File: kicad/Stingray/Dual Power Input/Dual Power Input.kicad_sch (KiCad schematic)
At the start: 16 parts, among them J2 Screw_Terminal_01x12, SW1 SW_SPST, U1 TMLM04115, U2 TMLM04115

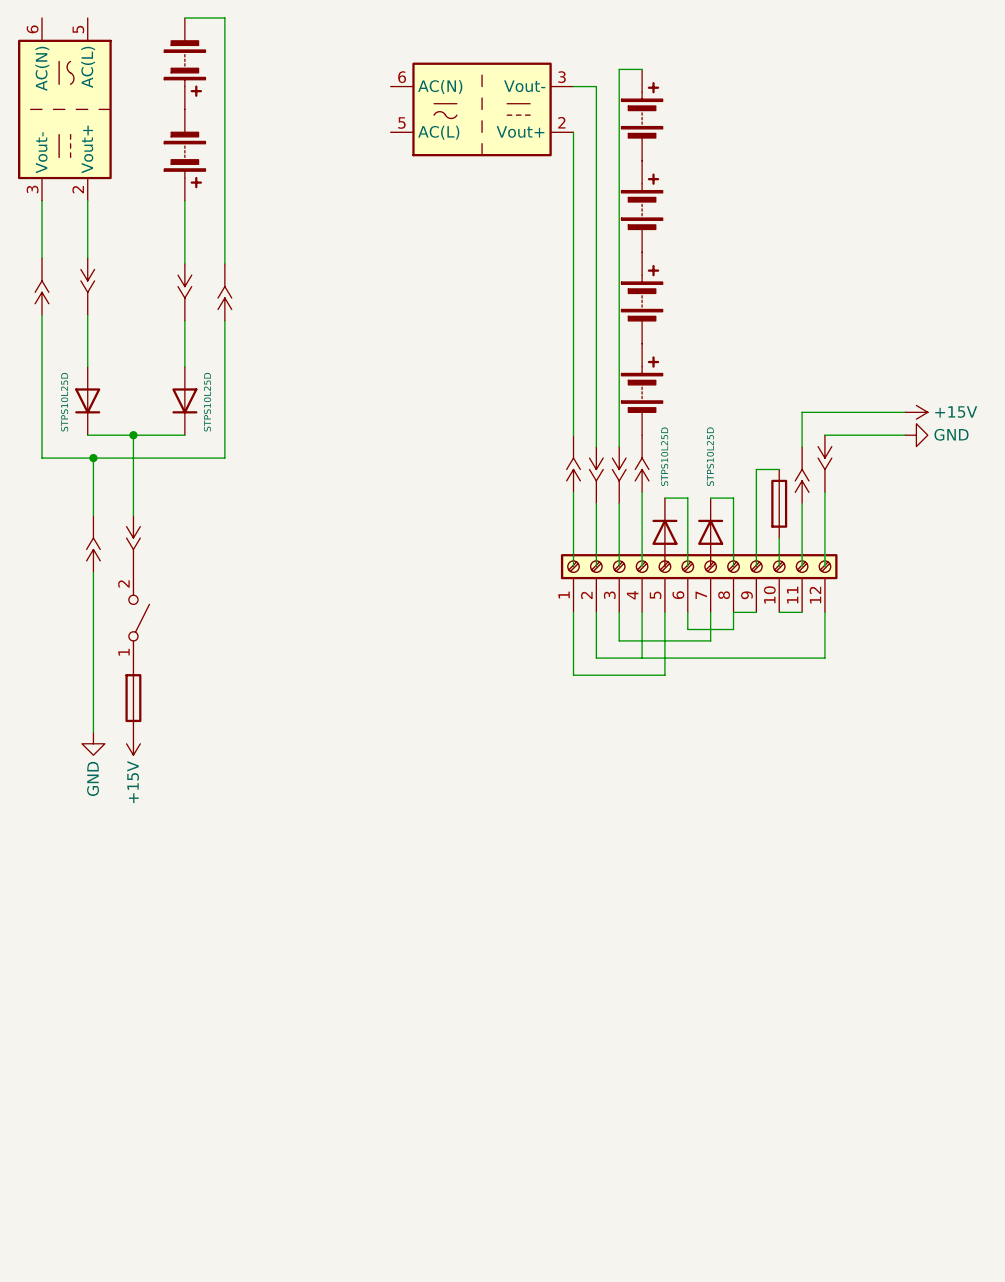
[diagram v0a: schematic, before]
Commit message: v1.2 amend 2026-09-21: right rear Power Input Panel rewire caught up
Manual:
- Ch 2.2 Protection line: 15SQ045 pair (was single STPS10L25D)
- Ch 3.1 Topology: header 'target/in progress' -> 'current, 2026-09-20',
  Status paragraph deleted; topology diode annotation swap to 15SQ045
  with terminal-strip cross-ref
- Ch 3.1 'Fuse-holder proto-board' section rewritten as 'Right rear
  Power Input Panel (2026-09-20, as-built)' - dual PowerPoles, panel
  fuse, 12-pos terminal strip carrying the OR-ing diode pair, RJ45
  keystone jack, bench diode-block field-verification note, four
  assembly photos in stingray build repo, KiCad source refs, and a
  short historical paragraph preserving the pre-rewire proto-board
- Ch 20 BOM Power section: 2 x 15SQ045 + terminal strip + dual
  PowerPole panel-mount + RJ45 keystone (replaces 1 x STPS10L25D)
- Appendix G.9: schematic bumped to 2026.09.20.png; subject updated
  with Dual Power Input panel description; source paths add sub-sheet
- Front-matter version bump 1.1 -> 1.2 with amendment summary

Field Notes:
- FN 22 heading: date list gains 'hardware caught up 2026-09-20'
- FN 22 body: STPS10L25D -> 15SQ045 in the OR-ing description
- FN 22 scope note extended: physical rewire installed 2026-09-20 as
  the right rear Power Input Panel; photos cited
- New FN 22 sub-section 'Part-number footnote': STPS10L25D was pre-
  rewire design intent; 15SQ045 (15 A / 45 V axial) installed for
  higher I/V margin and terminal-strip form factor
- New FN 22 sub-section 'Verifying the OR-ing block with a DMM':
  Sergei's tip explained - reverse-biased Schottky looks like
  ~100 kohm to the DMM's 10 Mohm input; parallel 10 kohm across the
  probes collapses the phantom-voltage reading to a few mV and
  confirms the block. Divider math included.

KiCad source (yesterday's uncommitted work):
- kicad/Stingray/Stingray.kicad_sch, .kicad_pro (top-level sheet)
- kicad/Stingray/Dual Power Input/*.kicad_sch, *.kicad_pro (new
  sub-project for the right re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
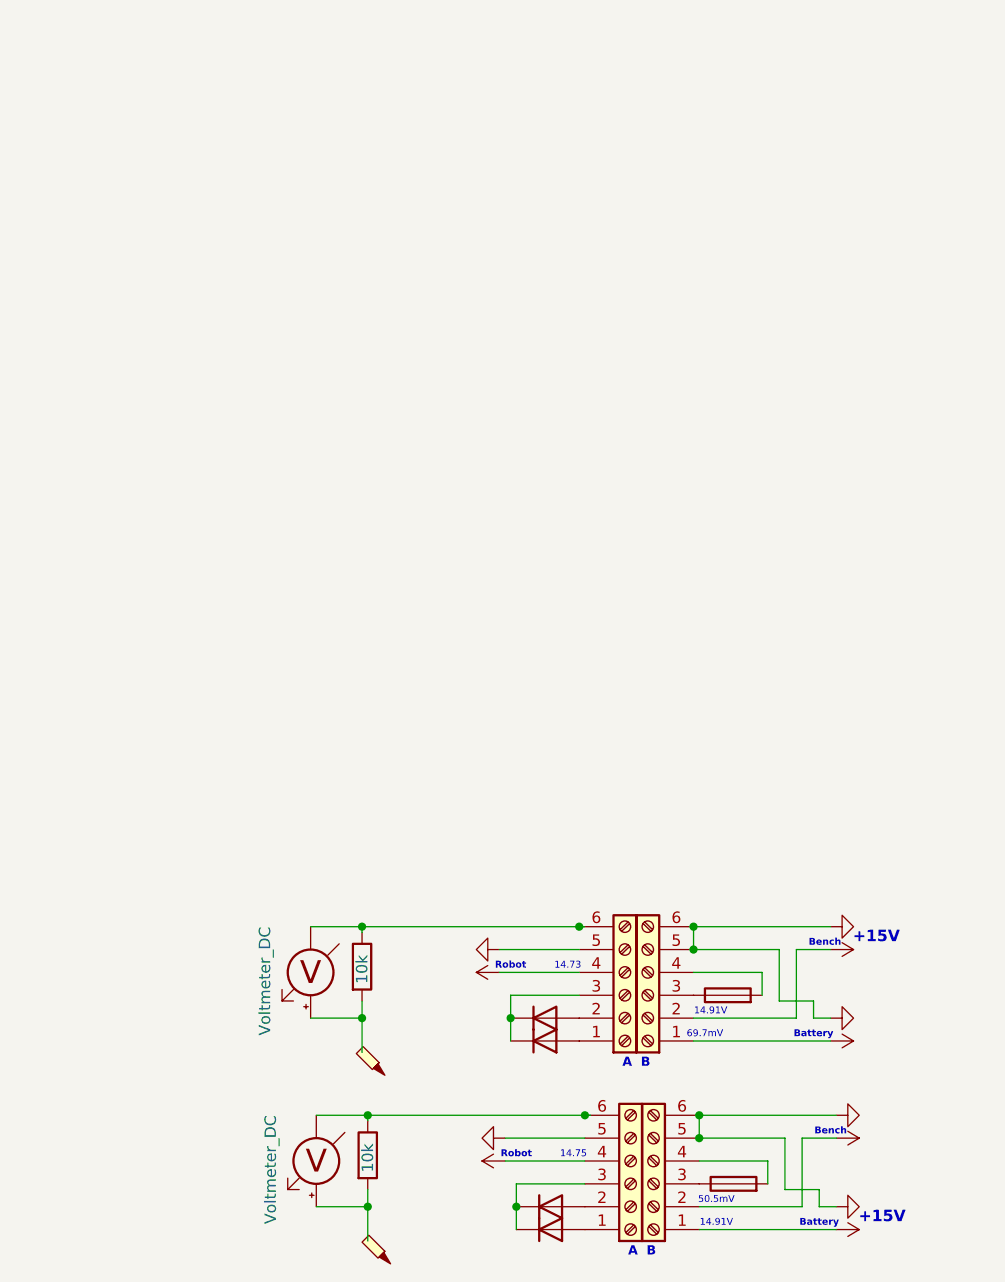
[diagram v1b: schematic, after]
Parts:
- removed BT1, BT2, BT3, BT4, BT5, BT6: Battery, symbol Device:Battery
- removed D1, D2, D3, D4: STPS10L25D, Diode_THT:D_DO-35_SOD27_P7.62mm_Horizontal, symbol Diode:1N914
- removed F1, F2: Fuse, symbol Device:Fuse
- removed J2: Screw_Terminal_01x12, symbol Connector:Screw_Terminal_01x12
- removed SW1: SW_SPST, symbol Switch:SW_SPST
- removed U1, U2: TMLM04115, Converter_ACDC:Converter_ACDC_TRACO_TMLM-04_THT, symbol Converter_ACDC:TMLM04115
- added D10, D11, D12, D9: STPS10L25D, Diode_THT:D_DO-35_SOD27_P7.62mm_Horizontal, symbol Diode:1N914
- added F5, F6: Fuse, symbol Device:Fuse
- added J10, J7, J8, J9: Screw_Terminal_01x06, symbol Connector:Screw_Terminal_01x06
- added MES3, MES4: Voltmeter_DC, symbol Device:Voltmeter_DC
- added R3, R4: 10k, symbol Device:R
- added TP3, TP4: TestPoint_Probe, symbol Connector:TestPoint_Probe
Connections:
- net +15V: now also J10.1 (Pin_1), J10.2 (Pin_2), J7.4 (Pin_4), J8.1 (Pin_1), J8.2 (Pin_2), J9.4 (Pin_4)
- new net: D10.2 (A), J7.1 (Pin_1)
- new net: D9.2 (A), J7.2 (Pin_2)
- new net: D10.1 (K), D9.1 (K), J7.3 (Pin_3)
- new net: J7.6 (Pin_6), MES3.1 (-), R3.1
- new net: D11.1 (K), D12.1 (K), J9.3 (Pin_3)
- new net: D12.2 (A), J9.1 (Pin_1)
- new net: F5.1, J8.3 (Pin_3)
- new net: F5.2, J8.4 (Pin_4)
- new net: MES3.2 (+), R3.2
- new net: J9.6 (Pin_6), MES4.1 (-), R4.1
- new net: MES4.2 (+), R4.2
- new net: F6.1, J10.3 (Pin_3)
- new net: F6.2, J10.4 (Pin_4)
- new net: D11.2 (A), J9.2 (Pin_2)
- new net GND: J10.5 (Pin_5), J10.6 (Pin_6), J7.5 (Pin_5), J8.5 (Pin_5), J8.6 (Pin_6), J9.5 (Pin_5)
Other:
- note added: "+15V"
- note added: "14.73"
- note added: "14.75"
- note added: "14.91V"
- note added: "50.5mV"
- note added: "69.7mV"
- note added: "A B"
- note added: "Battery"
- note added: "Bench"
- note added: "Robot"
